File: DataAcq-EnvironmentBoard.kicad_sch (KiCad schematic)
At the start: 41 parts, among them J1 Airflow Breakout, J2 CAN Output, J3 CAN Input, J4 Humidity Breakout, J5 Temp Breakout, U1 SHT45, U2 FS3000-1005, U3 LMT87DCK, U4 Daughterboard Connector

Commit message: pls be the last time i have to layout this
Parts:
- removed TP6, TP7, TP8, TP9: TestPoint, Connector_PinHeader_2.54mm:PinHeader_1x01_P2.54mm_Vertical, symbol Connector:TestPoint
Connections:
- net I2C1_SCL: now also J4.3 (Pin_3); no longer J4.2 (Pin_2)
- net I2C1_SDA: now also J4.2 (Pin_2); no longer J4.3 (Pin_3)

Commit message: update BOM
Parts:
- J1, J4: P/N (none) -> 436500244
- J5: P/N (none) -> 436500315
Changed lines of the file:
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@@
+			)
+		)
+		(property "P/N" "436500315"
+			(at 167.64 184.15 0)
+			(effects
+				(font
+					(size 1.27 1.27)
+				)
+				(hide yes)
 			)
 		)
@@
 			)
 		)
-		(property "P/N" " "
+		(property "P/N" "436500244"
 			(at 132.08 190.5 0)
 			(effects
@@
 			(at 130.81 160.02 0)
 			(effects
+				(font
+					(size 1.27 1.27)
+				)
+				(hide yes)
+			)
+		)
+		(property "P/N" "436500244"
+			(at 130.81 160.02 0)
+			(effects

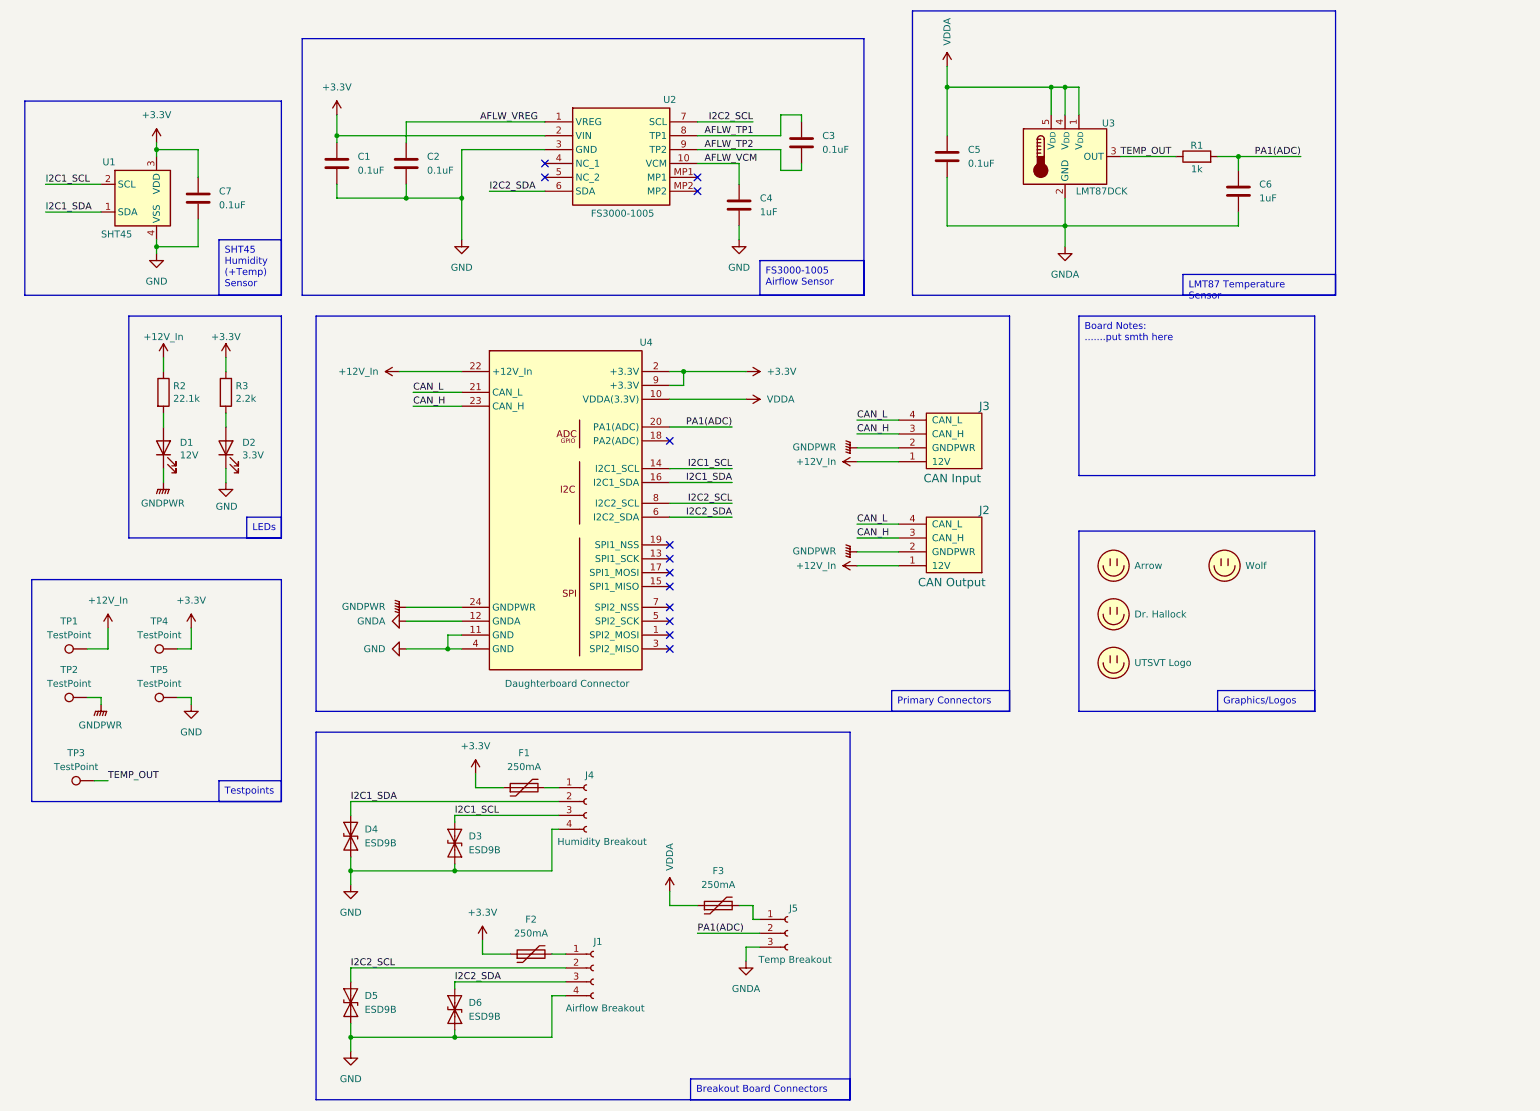
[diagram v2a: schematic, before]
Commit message: start sch/layout modifications
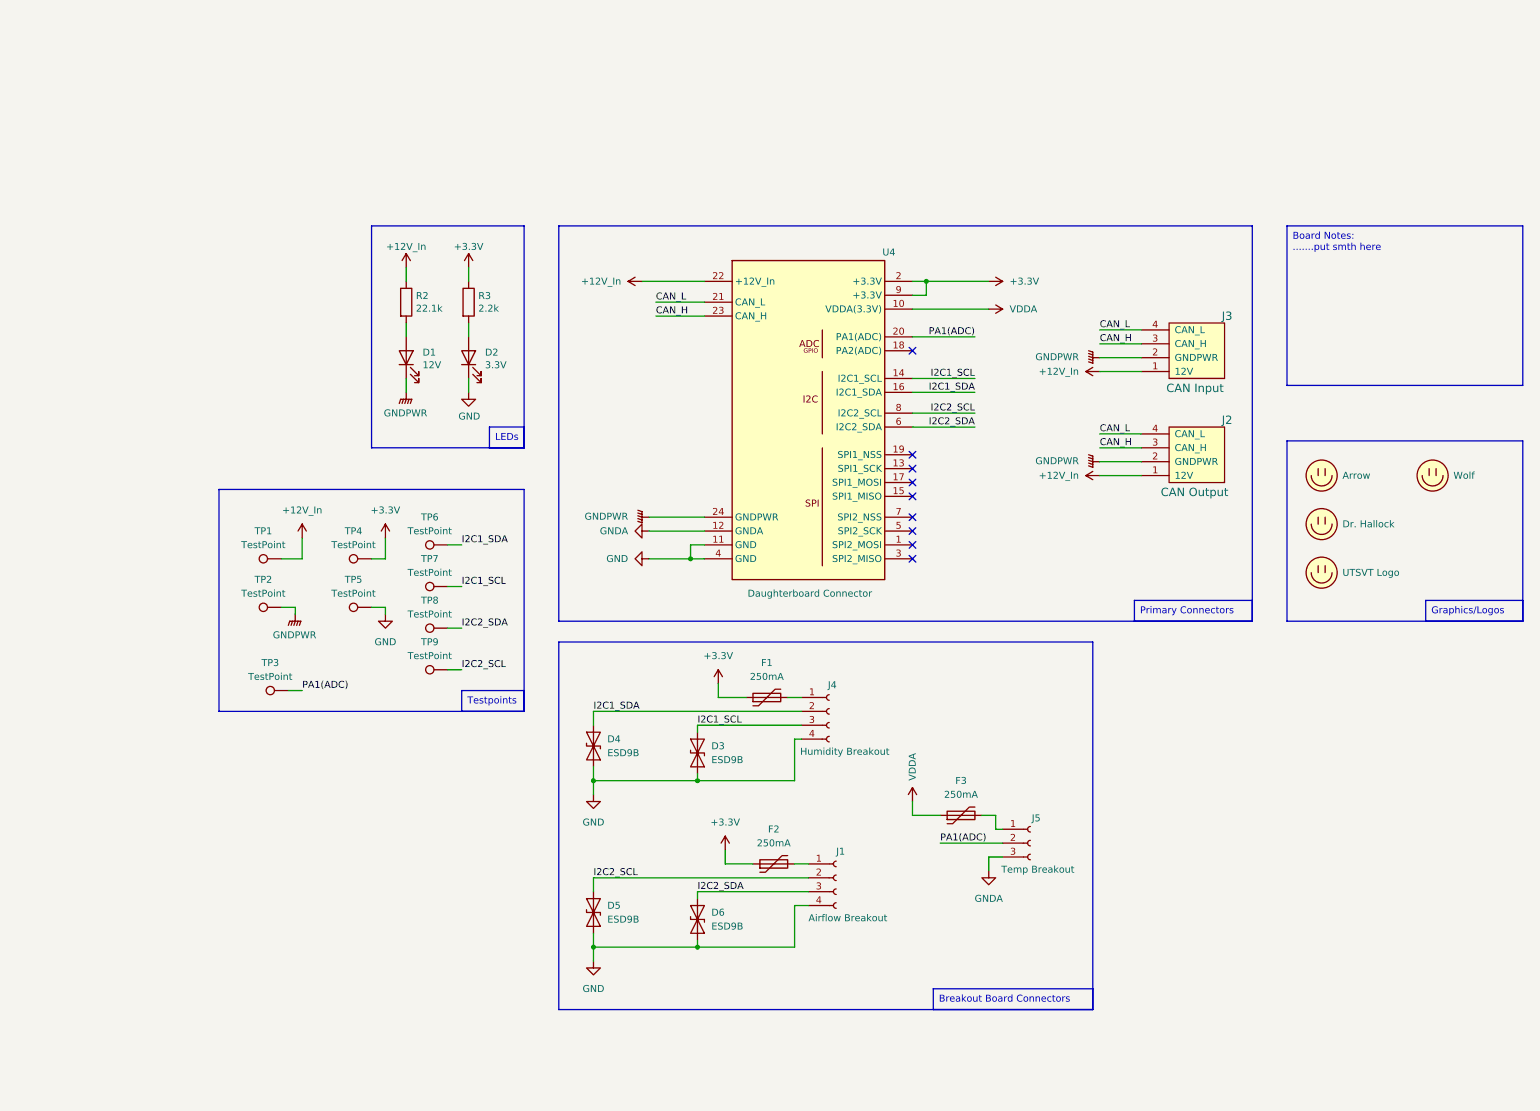
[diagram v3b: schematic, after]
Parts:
- removed C1, C2, C3, C5, C7: 0.1uF, Capacitor_SMD:C_0805_2012Metric, symbol Device:C
- removed C4, C6: 1uF, Capacitor_SMD:C_0805_2012Metric, symbol Device:C
- removed R1: 1k, Resistor_SMD:R_0805_2012Metric, symbol Device:R
- removed U1: SHT45, Sensor_Humidity:Sensirion_DFN-4_1.5x1.5mm_P0.8mm_SHT4x_NoCentralPad, symbol Sensor_Humidity:SHT4x
- removed U2: FS3000-1005, SamacSys_Parts:FS30001005, symbol SamacSys_Parts:FS3000-1005
- removed U3: LMT87DCK, Package_TO_SOT_SMD:SOT-353_SC-70-5, symbol Sensor_Temperature:LMT87DCK
- added TP6, TP7, TP8, TP9: TestPoint, Connector_PinHeader_2.54mm:PinHeader_1x01_P2.54mm_Vertical, symbol Connector:TestPoint
- TP3: footprint UTSVT_Special:TestPoint_HEX_3mmID -> Connector_PinHeader_2.54mm:PinHeader_1x01_P2.54mm_Vertical
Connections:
- net TEMP_OUT is gone; now on net PA1(ADC): TP3.1
- net I2C1_SCL: now also TP7.1
- net I2C1_SDA: now also TP6.1
- net I2C2_SCL: now also TP9.1
- net I2C2_SDA: now also TP8.1
- no-connect marks 13 -> 9
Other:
- moved on the sheet: D1, D2, D3, D4, D5, D6, F1, F2, F3, J1, J2, J3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

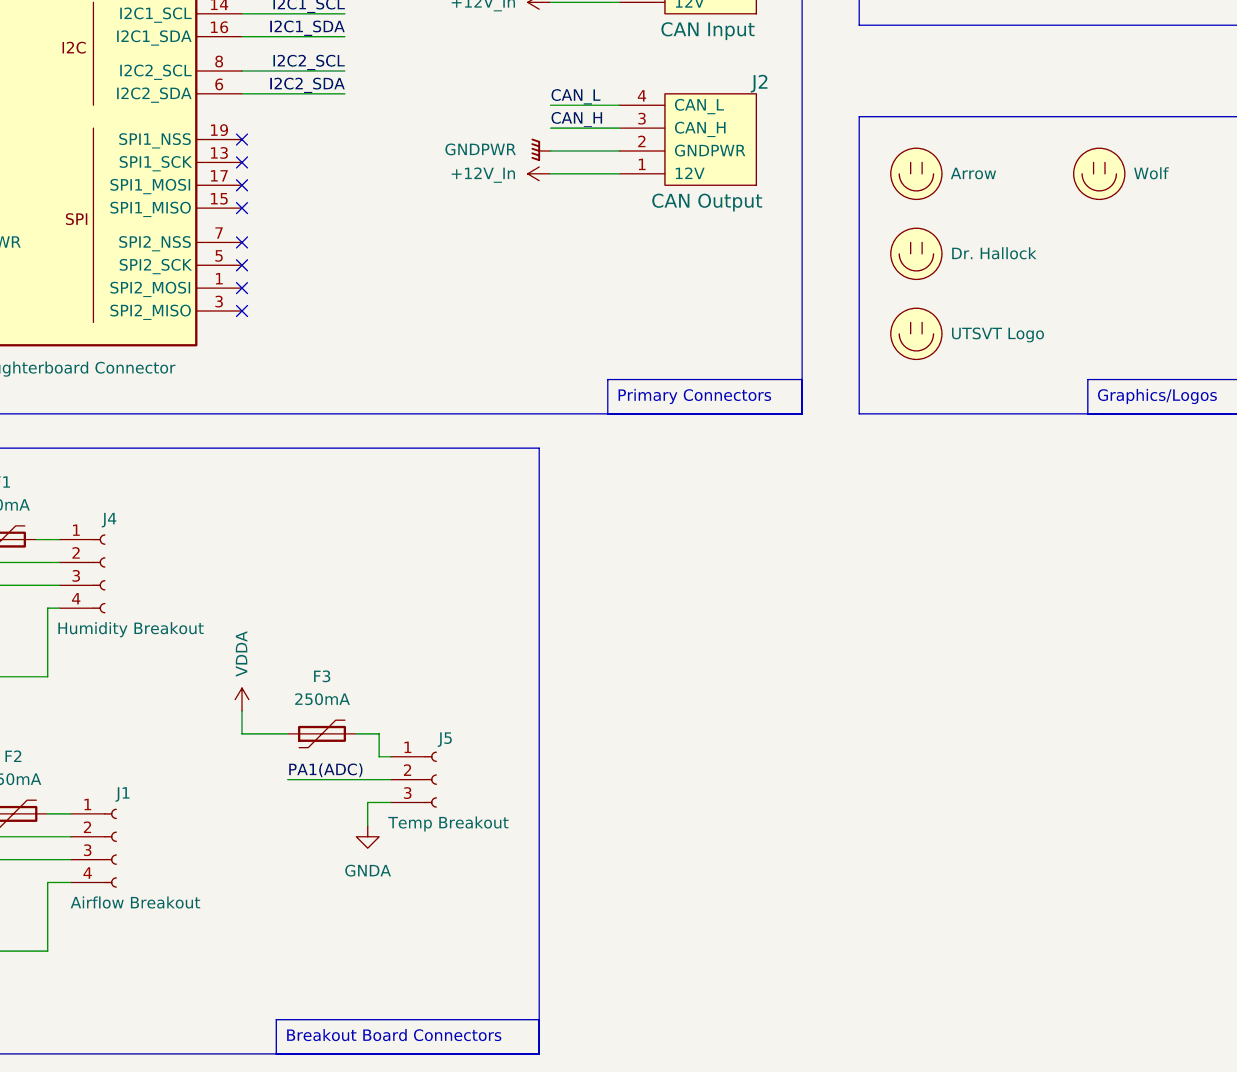
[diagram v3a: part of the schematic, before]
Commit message: update BOM and model
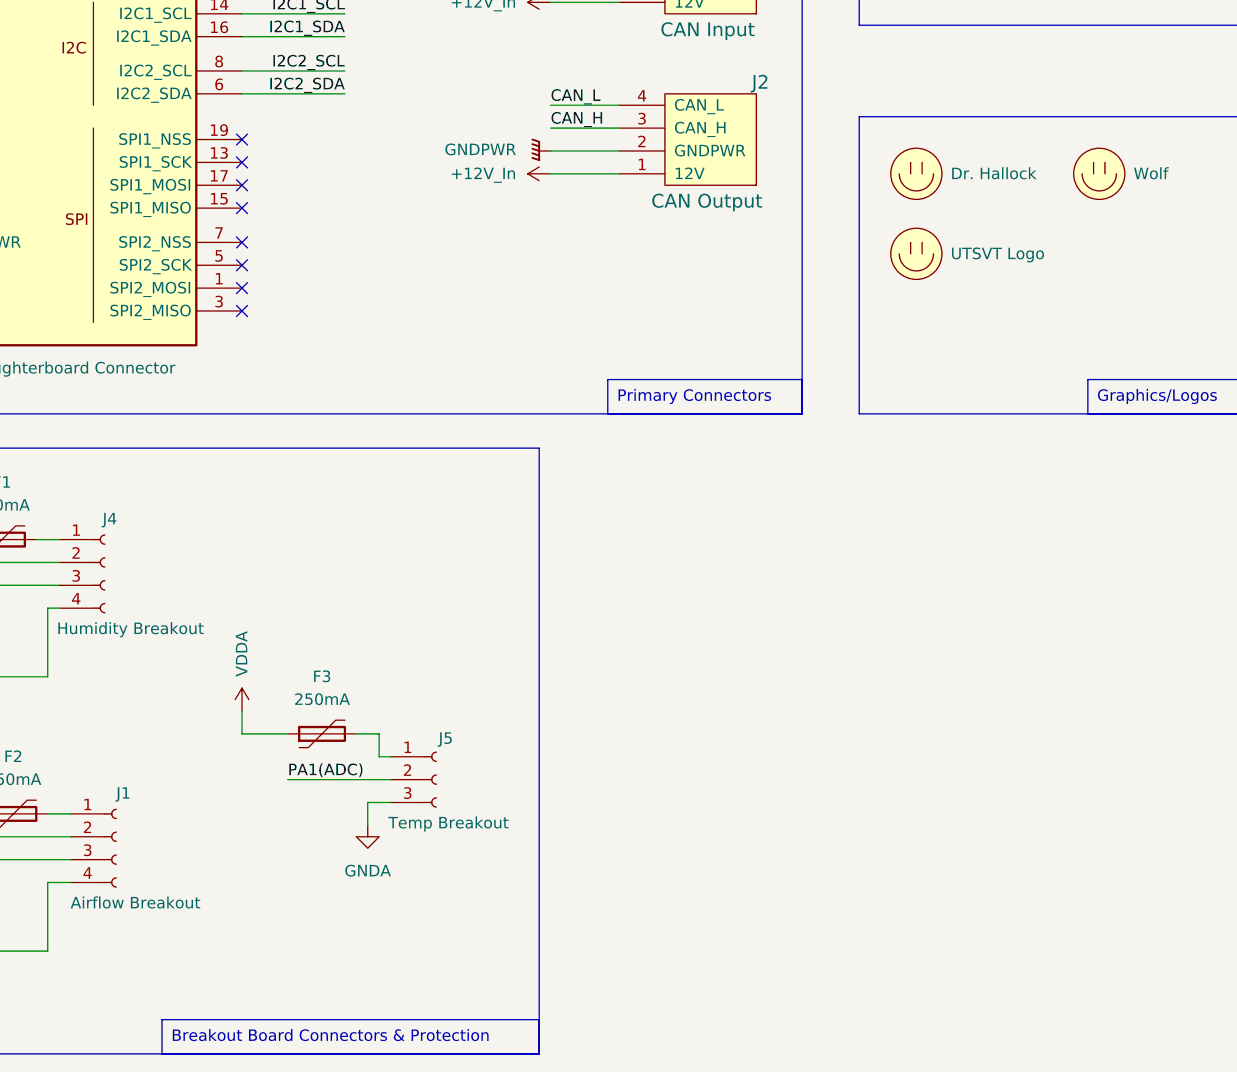
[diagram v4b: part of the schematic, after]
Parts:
- removed LOGO1: Arrow, images:arrow, symbol utsvt-misc:Logo_Placeholder
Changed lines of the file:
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@@
 		)
 	)
-	(text_box "Breakout Board Connectors"
+	(text_box "Breakout Board Connectors & Protection"
 		(exclude_from_sim no)
-		(at 194.31 194.31 0)
-		(size 29.21 3.81)
+		(at 181.61 194.31 0)
+		(size 41.91 3.81)
 		(stroke
 			(width 0)
@@
 	(symbol
 		(lib_id "utsvt-misc:Logo_Placeholder")
-		(at 265.43 118.11 0)
+		(at 265.43 109.22 0)
 		(unit 1)
 		(exclude_from_sim no)
@@
 		(fields_autoplaced yes)
 		(property "Reference" "LOGO3"
-			(at 265.43 114.3 0)
+			(at 265.43 105.41 0)
 			(effects
 				(font
@@
 		)
 		(property "Value" "UTSVT Logo"
-			(at 269.24 118.1099 0)
+			(at 269.24 109.2199 0)
 			(effects
 				(font
@@
 		)
 		(property "Footprint" "UTSVT_Special:UTSVT_Logo_Symbol"
-			(at 265.43 116.205 0)
+			(at 265.43 107.315 0)
 			(effects
 				(font
@@
 		)
 		(property "Datasheet" ""
-			(at 265.43 116.205 0)
+			(at 265.43 107.315 0)
 			(effects
 				(font
@@
 		)
 		(property "Description" "Graph footprint placeholder"
-			(at 265.43 118.11 0)
+			(at 265.43 109.22 0)
 			(effects
 				(font
@@
 	(symbol
 		(lib_id "utsvt-misc:Logo_Placeholder")
-		(at 265.43 109.22 0)
+		(at 265.43 100.33 0)
 		(unit 1)
 		(exclude_from_sim no)
@@
 		(fields_autoplaced yes)
 		(property "Reference" "LOGO2"
-			(at 265.43 105.41 0)
+			(at 265.43 96.52 0)
 			(effects
 				(font
@@
 		)
 		(property "Value" "Dr. Hallock"
-			(at 269.24 109.2199 0)
+			(at 269.24 100.3299 0)
 			(effects
 				(font
@@
 		)
 		(property "Footprint" "UTSVT_Special:Hallock_Image_Tiny"
-			(at 265.43 107.315 0)
+			(at 265.43 98.425 0)
 			(effects
 				(font
@@
 		)
 		(property "Datasheet" ""
-			(at 265.43 107.315 0)
+			(at 265.43 98.425 0)
 			(effects
 				(font
@@
 		)
 		(property "Description" "Graph footprint placeholder"
-			(at 265.43 109.22 0)
+			(at 265.43 100.33 0)
 			(effects
 				(font
@@
 					(unit 1)
 				)
-			)
-		)
-	)
-	(symbol
-		(lib_id "utsvt-misc:Logo_Placeholder")
-		(at 265.43 100.33 0)
-		(unit 1)
-		(exclude_from_sim no)
-		(in_bom yes)
-		(on_board yes)
-		(dnp no)
-		(fields_autoplaced yes)
-		(property "Reference" "LOGO1"
-			(at 265.43 96.52 0)
-			(effects
-				(font
-					(size 1.27 1.27)
-				)
-				(hide yes)
-			)
-		)
-		(property "Value" "Arrow"
-			(at 269.24 100.3299 0)
-			(effects
-				(font
-					(size 1.27 1.27)
-				)
-				(justify left)
-			)
-		)
-		(property "Footprint" "images:arrow"
-			(at 265.43 98.425 0)
-			(effects
-				(font
-					(size 1.27 1.27)
-				)
-				(hide yes)
-			)
-		)
-		(property "Datasheet" ""
-			(at 265.43 98.425 0)
-			(effects
-				(font
-					(size 1.27 1.27)
-				)
-				(hide yes)
-			)
-		)
-		(property "Description" "Graph footprint placeholder"
-			(at 265.43 100.33 0)
-			(effects
-				(font
-					(size 1.27 1.27)
-				)
-				(hide yes)
-			)
-		)
-		(instances
-			(project ""
-				(path "/bc5fb1f8-c603-414b-89d1-18cc156ddb66"
-					(reference "LOGO1")
-					(unit 1)
-				)
